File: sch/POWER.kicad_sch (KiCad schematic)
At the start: 32 parts, among them Q1 NTD2955T4G, Q2 IRLML0060, Q3 IRLML0060, U5 AP63205WU-7, U6 LD1117S33CTR

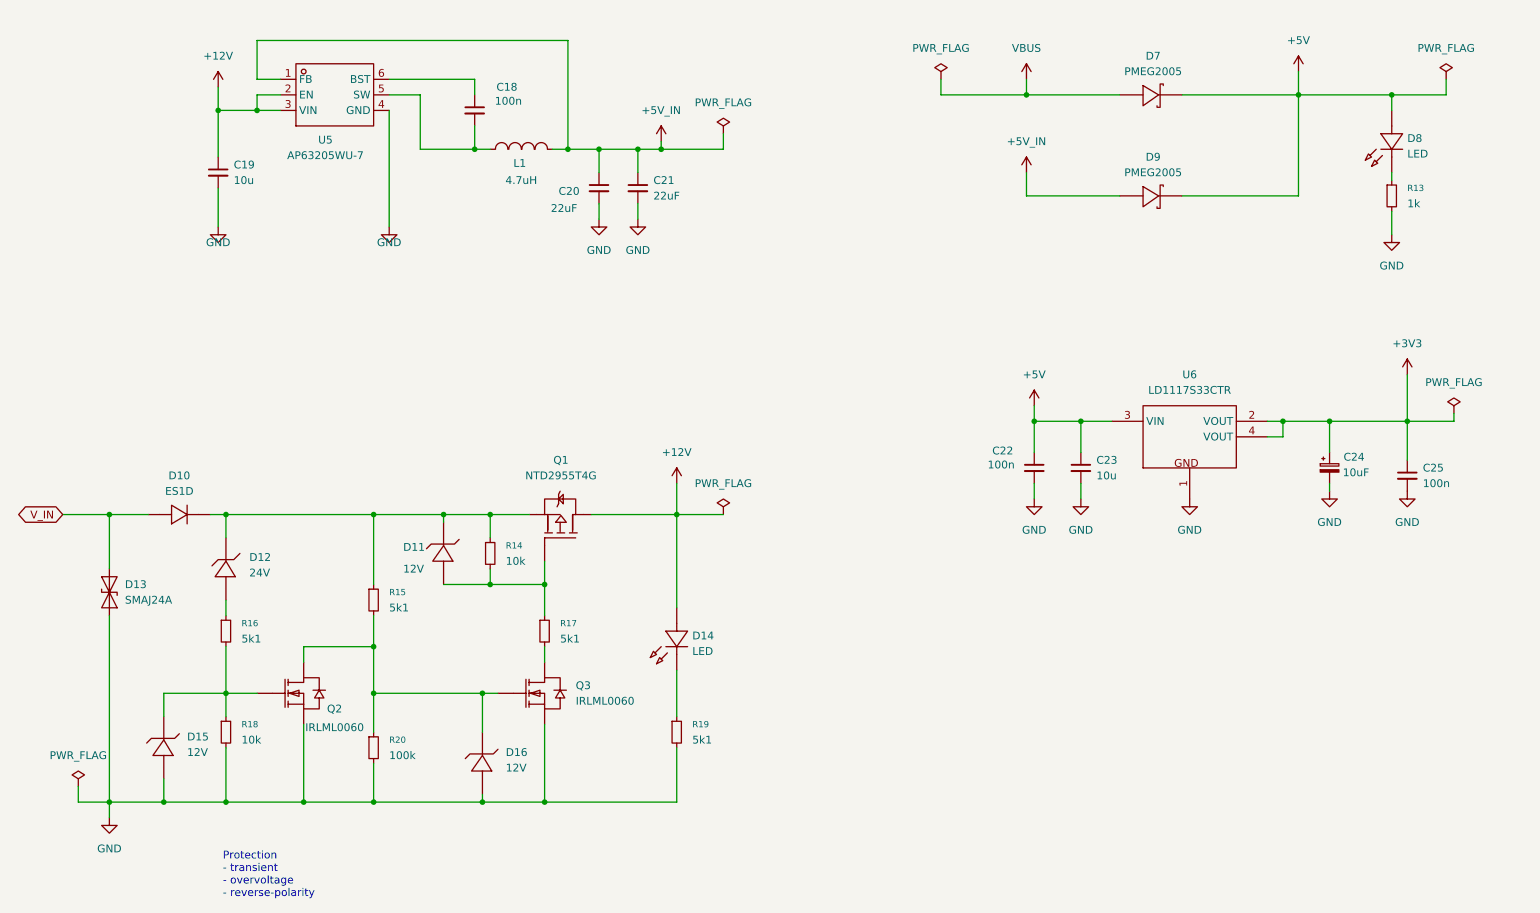
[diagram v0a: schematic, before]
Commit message: Fix SPI pins add 3.3v led
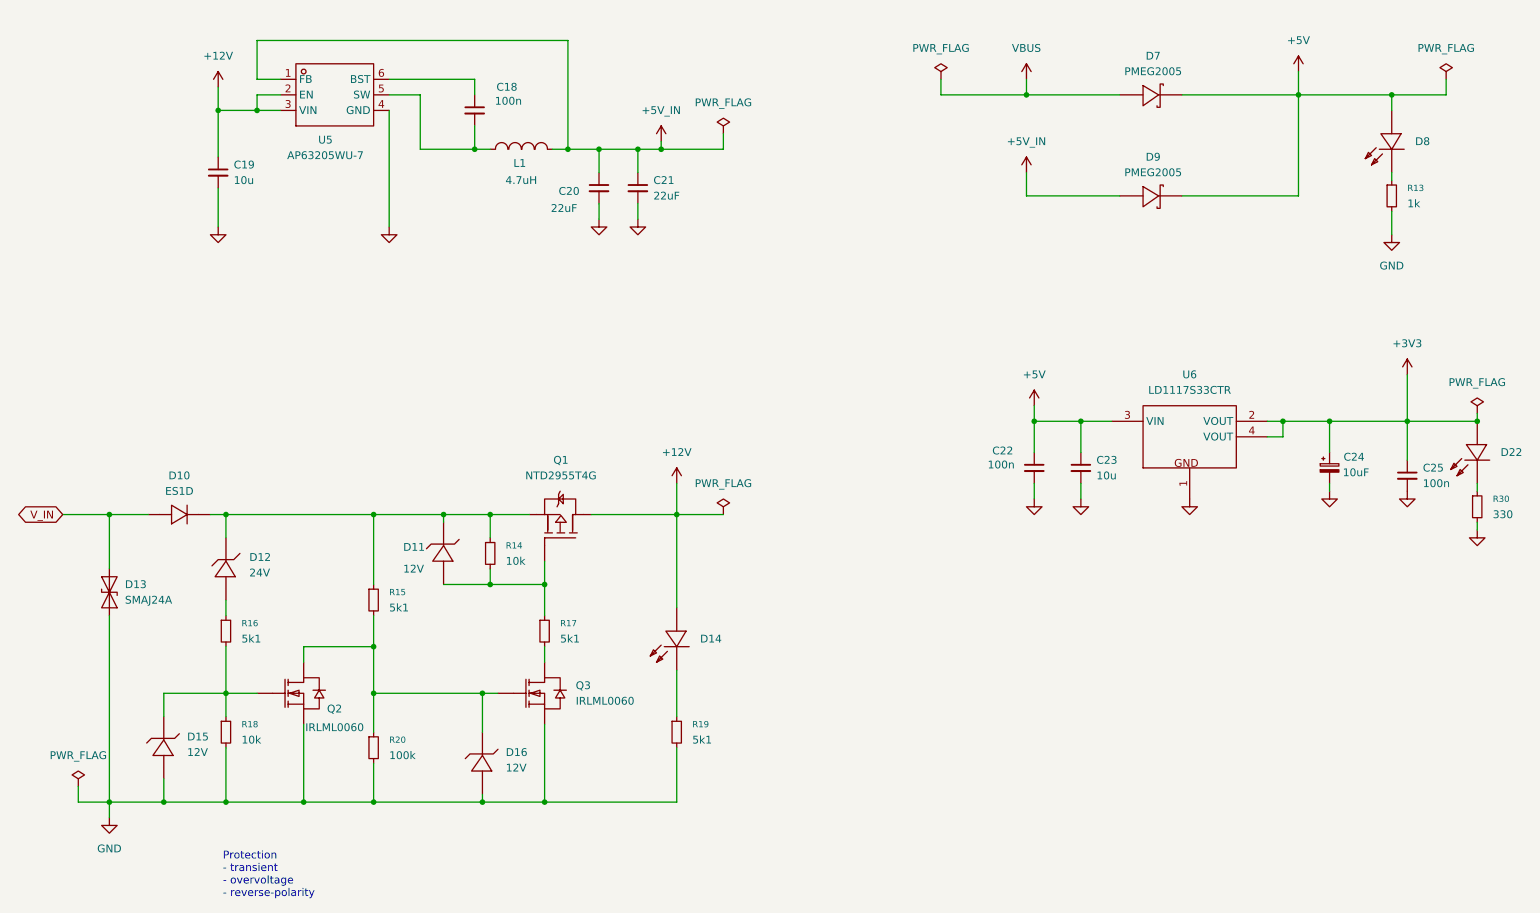
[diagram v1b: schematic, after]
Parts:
- removed D14, D8: LED, EasyEDA_Lib:LED0805-RD_GREEN, symbol EasyEDA_Lib:XL-2012UGC
- added D14, D22, D8: ~, EasyEDA_Lib:LED0603-RD, symbol EasyEDA_Lib:KT-0603R
- added R30: 330, EasyEDA_Lib:R0603, symbol Device:R_Small
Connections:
- net +12V: now also D14.2 (A)
- net +3V3: now also D22.2 (A)
- net +5V: now also D8.2 (A)
- net GND: now also R30.2
- net at R13.1: now also D8.1 (K)
- net at R19.1: now also D14.1 (K)
- new net: D22.1 (K), R30.1

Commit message: change 2x22u to 3x10u plot all order jlcpcb + lcsc
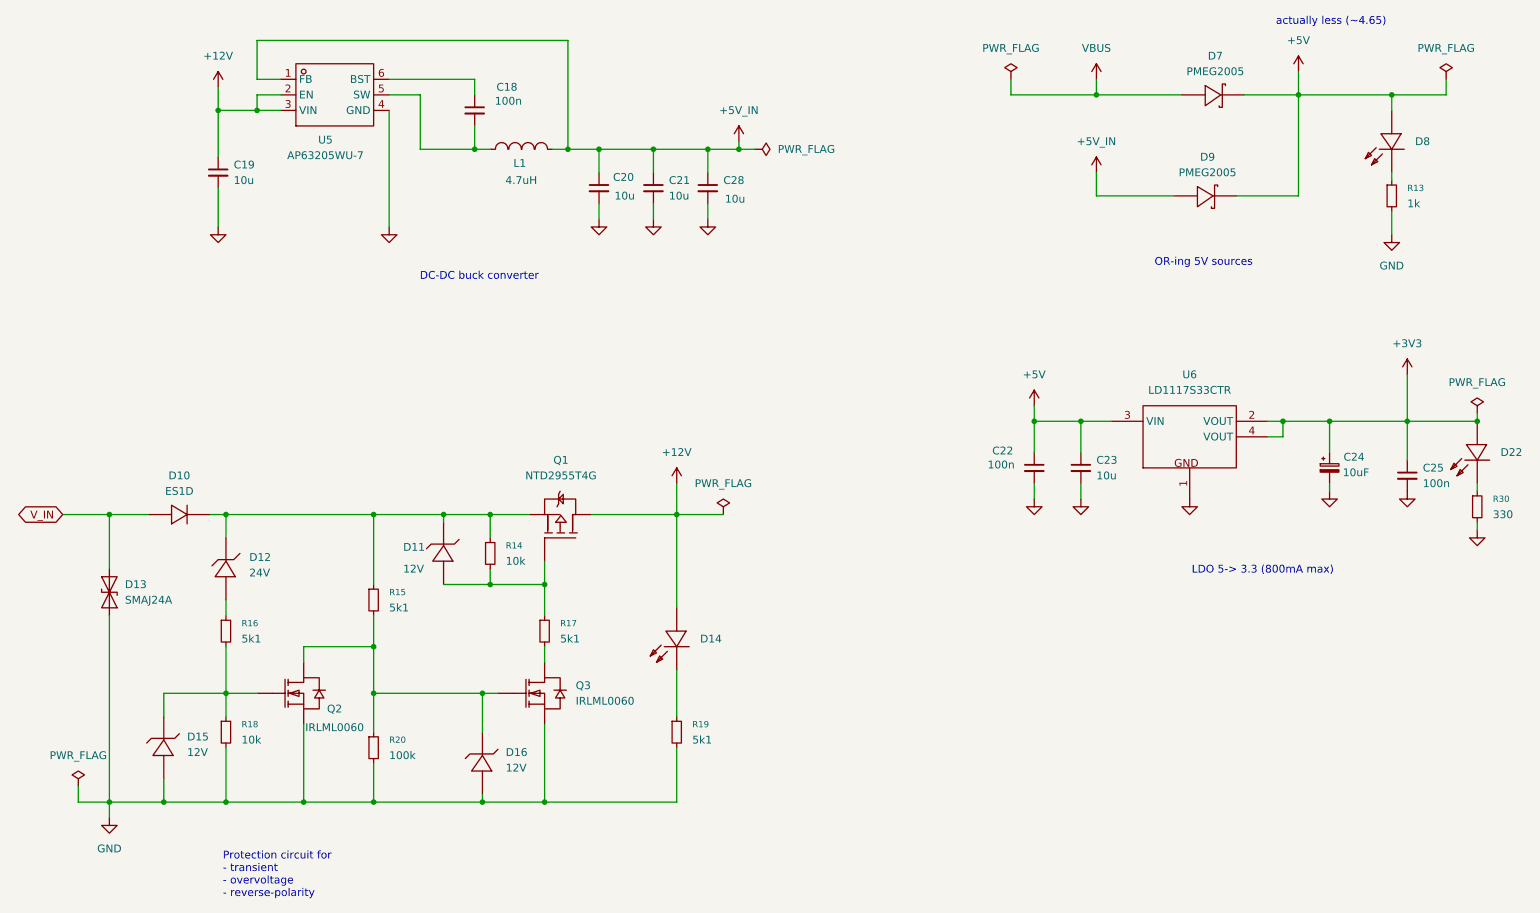
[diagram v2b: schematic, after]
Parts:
- added C28: 10u, EasyEDA_Lib:C0805, symbol Device:C_Small
- C20, C21: value 22uF -> 10u; footprint canlogger_custom_lib:C1206 -> EasyEDA_Lib:C0805; Supplier Part C12891 -> C15850
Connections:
- net +5V_IN: now also C28.1
- net GND: now also C28.2
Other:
- note added: "DC-DC buck converter"
- note added: "LDO 5-> 3.3 (800mA max)"
- note added: "OR-ing 5V sources"
- note added: "Protection circuit for - transient - overvoltage - reverse-polarity"
- note added: "actually less (~4.65)"
- note removed: "Protection - transient - overvoltage - reverse-polarity"
- moved on the sheet: D7, D9
